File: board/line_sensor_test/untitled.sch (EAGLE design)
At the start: 92 parts, among them U1 74HC4067SSOP-24, U2 74HC4067SSOP-24

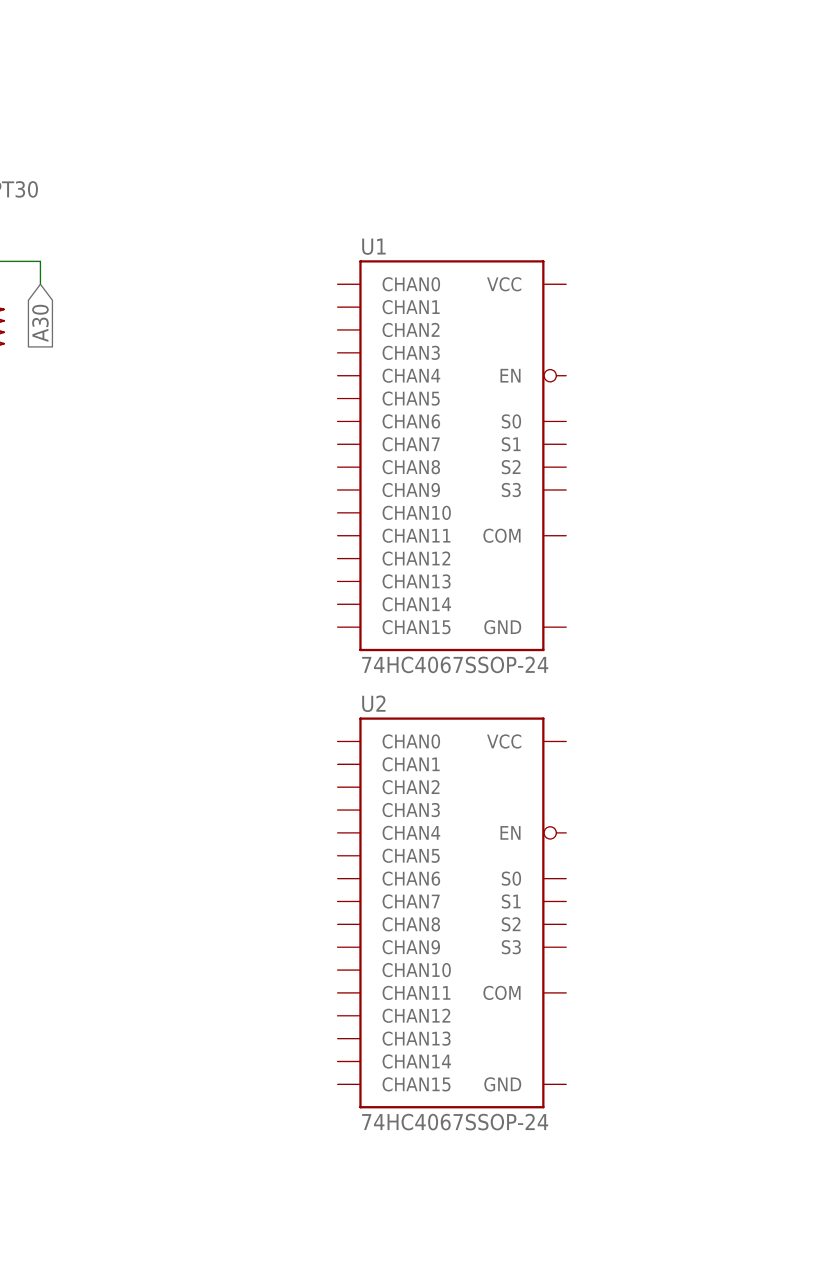
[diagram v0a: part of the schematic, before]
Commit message: making linesonsor_2
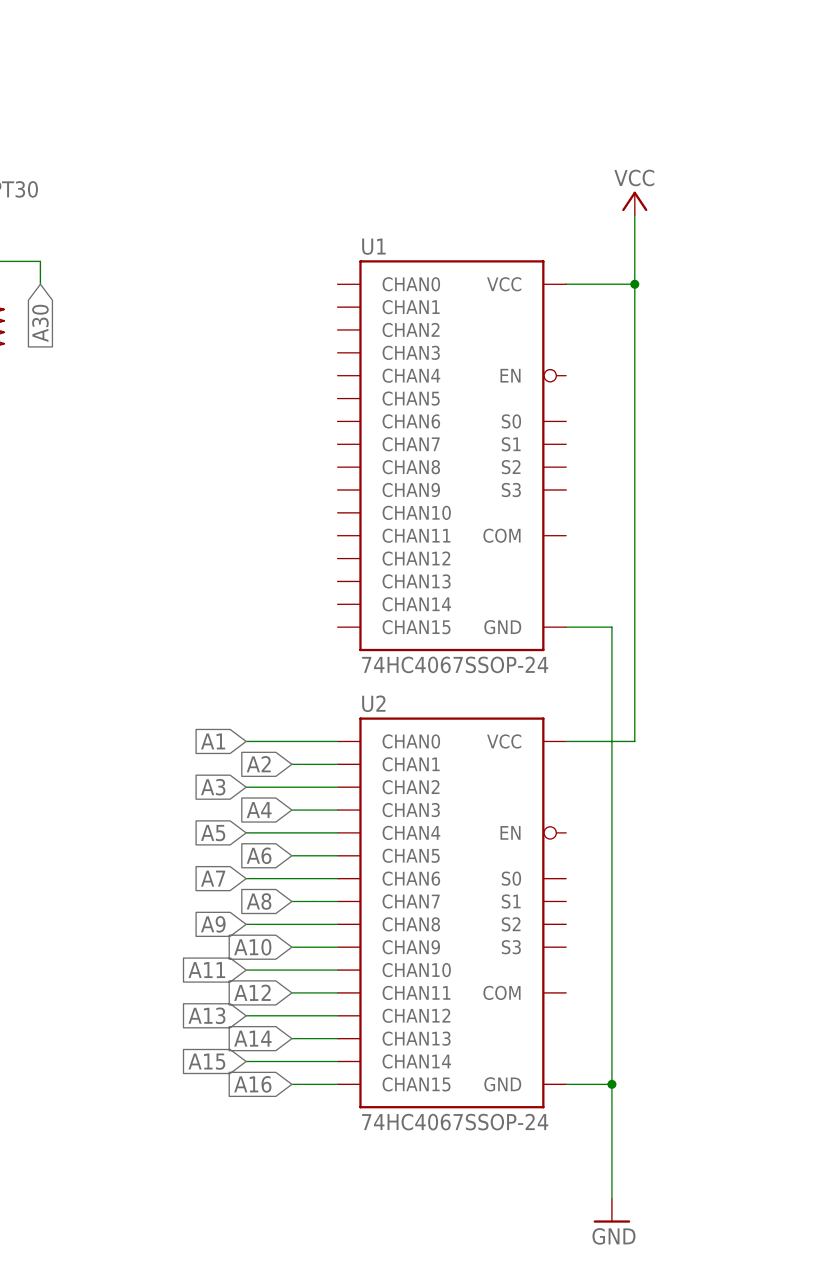
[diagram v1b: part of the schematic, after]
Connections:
- net A1: now also U2.CHAN0
- net A10: now also U2.CHAN9
- net A11: now also U2.CHAN10
- net A12: now also U2.CHAN11
- net A13: now also U2.CHAN12
- net A14: now also U2.CHAN13
- net A15: now also U2.CHAN14
- net A16: now also U2.CHAN15
- net A2: now also U2.CHAN1
- net A3: now also U2.CHAN2
- net A4: now also U2.CHAN3
- net A5: now also U2.CHAN4
- net A6: now also U2.CHAN5
- net A7: now also U2.CHAN6
- net A8: now also U2.CHAN7
- net A9: now also U2.CHAN8
- net GND: now also U1.GND, U2.GND
- net VCC: now also U1.VCC, U2.VCC
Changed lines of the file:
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@@
 <part name="U1" library="74HC4067" deviceset="74HC4067" device="SSOP-24"/>
 <part name="U2" library="74HC4067" deviceset="74HC4067" device="SSOP-24"/>
+<part name="U$3" library="supply" deviceset="VCC" device=""/>
+<part name="GND3" library="supply" deviceset="GND" device=""/>
 </parts>
 <sheets>
@@
 <attribute name="VALUE" x="365.76" y="-99.06" size="1.778" layer="95"/>
 </instance>
+<instance part="U$3" gate="G$1" x="396.24" y="5.08" smashed="yes">
+<attribute name="VALUE" x="393.954" y="5.842" size="1.778" layer="96" font="vector"/>
+</instance>
+<instance part="GND3" gate="1" x="393.7" y="-109.22" smashed="yes">
+<attribute name="VALUE" x="391.414" y="-111.76" size="1.778" layer="96" font="vector"/>
+</instance>
 </instances>
 <busses>
@@
 <label x="35.56" y="-5.08" size="1.778" layer="95" rot="R270" xref="yes"/>
 </segment>
+<segment>
+<pinref part="U2" gate="G$1" pin="CHAN0"/>
+<wire x1="363.22" y1="-55.88" x2="353.06" y2="-55.88" width="0.1524" layer="91"/>
+<label x="353.06" y="-55.88" size="1.778" layer="95" rot="R180" xref="yes"/>
+</segment>
 </net>
 <net name="A2" class="0">
@@
 <junction x="40.64" y="-2.54"/>
 </segment>
+<segment>
+<pinref part="U2" gate="G$1" pin="CHAN1"/>
+<wire x1="363.22" y1="-58.42" x2="358.14" y2="-58.42" width="0.1524" layer="91"/>
+<label x="358.14" y="-58.42" size="1.778" layer="95" rot="R180" xref="yes"/>
+</segment>
 </net>
 <net name="A3" class="0">
@@
 <junction x="50.8" y="-2.54"/>
 </segment>
+<segment>
+<pinref part="U2" gate="G$1" pin="CHAN2"/>
+<wire x1="363.22" y1="-60.96" x2="353.06" y2="-60.96" width="0.1524" layer="91"/>
+<label x="353.06" y="-60.96" size="1.778" layer="95" rot="R180" xref="yes"/>
+</segment>
 </net>
 <net name="A4" class="0">
@@
 <wire x1="66.04" y1="-2.54" x2="66.04" y2="-5.08" width="0.1524" layer="91"/>
 </segment>
+<segment>
+<pinref part="U2" gate="G$1" pin="CHAN3"/>
+<wire x1="363.22" y1="-63.5" x2="358.14" y2="-63.5" width="0.1524" layer="91"/>
+<label x="358.14" y="-63.5" size="1.778" layer="95" rot="R180" xref="yes"/>
+</segment>
 </net>
 <net name="A5" class="0">
@@
 <junction x="71.12" y="-2.54"/>
 <wire x1="76.2" y1="-2.54" x2="76.2" y2="-5.08" width="0.1524" layer="91"/>
+</segment>
+<segment>
+<pinref part="U2" gate="G$1" pin="CHAN4"/>
+<wire x1="363.22" y1="-66.04" x2="353.06" y2="-66.04" width="0.1524" layer="91"/>
+<label x="353.06" y="-66.04" size="1.778" layer="95" rot="R180" xref="yes"/>
 </segment>
 </net>
@@
 <junction x="635" y="81.28"/>
 </segment>
+<segment>
+<pinref part="U2" gate="G$1" pin="VCC"/>
+<wire x1="388.62" y1="-55.88" x2="396.24" y2="-55.88" width="0.1524" layer="91"/>
+<wire x1="396.24" y1="-55.88" x2="396.24" y2="-5.08" width="0.1524" layer="91"/>
+<pinref part="U1" gate="G$1" pin="VCC"/>
+<wire x1="396.24" y1="2.54" x2="396.24" y2="-5.08" width="0.1524" layer="91"/>
+<wire x1="396.24" y1="-5.08" x2="388.62" y2="-5.08" width="0.1524" layer="91"/>
+<junction x="396.24" y="-5.08"/>
+<pinref part="U$3" gate="G$1" pin="VCC"/>
+</segment>
 </net>
 <net name="A6" class="0">
@@
 <junction x="81.28" y="-2.54"/>
 </segment>
+<segment>
+<pinref part="U2" gate="G$1" pin="CHAN5"/>
+<wire x1="363.22" y1="-68.58" x2="358.14" y2="-68.58" width="0.1524" layer="91"/>
+<label x="358.14" y="-68.58" size="1.778" layer="95" rot="R180" xref="yes"/>
+</segment>
 </net>
 <net name="A7" class="0">
@@
 <wire x1="96.52" y1="-2.54" x2="96.52" y2="-5.08" width="0.1524" layer="91"/>
 </segment>
+<segment>
+<pinref part="U2" gate="G$1" pin="CHAN6"/>
+<wire x1="363.22" y1="-71.12" x2="353.06" y2="-71.12" width="0.1524" layer="91"/>
+<label x="353.06" y="-71.12" size="1.778" layer="95" rot="R180" xref="yes"/>
+</segment>
 </net>
 <net name="A8" class="0">
@@
 <junction x="101.6" y="-2.54"/>
 </segment>
+<segment>
+<label x="358.14" y="-73.66" size="1.778" layer="95" rot="R180" xref="yes"/>
+<wire x1="360.5276" y1="-73.66" x2="358.14" y2="-73.66" width="0.1524" layer="91"/>
+<pinref part="U2" gate="G$1" pin="CHAN7"/>
+<wire x1="360.5276" y1="-73.66" x2="363.22" y2="-73.66" width="0.1524" layer="91"/>
+</segment>
 </net>
 <net name="A9" class="0">
@@
 <junction x="111.76" y="-2.54"/>
 </segment>
+<segment>
+<pinref part="U2" gate="G$1" pin="CHAN8"/>
+<wire x1="363.22" y1="-76.2" x2="353.06" y2="-76.2" width="0.1524" layer="91"/>
+<label x="353.06" y="-76.2" size="1.778" layer="95" rot="R180" xref="yes"/>
+</segment>
 </net>
 <net name="A10" class="0">
@@
 <junction x="121.92" y="-2.54"/>
 </segment>
+<segment>
+<pinref part="U2" gate="G$1" pin="CHAN9"/>
+<wire x1="363.22" y1="-78.74" x2="358.14" y2="-78.74" width="0.1524" layer="91"/>
+<label x="358.14" y="-78.74" size="1.778" layer="95" rot="R180" xref="yes"/>
+</segment>
 </net>
 <net name="A11" class="0">
@@
 <junction x="132.08" y="-2.54"/>
 </segment>
+<segment>
+<pinref part="U2" gate="G$1" pin="CHAN10"/>
+<wire x1="363.22" y1="-81.28" x2="353.06" y2="-81.28" width="0.1524" layer="91"/>
+<label x="353.06" y="-81.28" size="1.778" layer="95" rot="R180" xref="yes"/>
+</segment>
 </net>
 <net name="A12" class="0">
@@
 <junction x="142.24" y="-2.54"/>
 </segment>
+<segment>
+<pinref part="U2" gate="G$1" pin="CHAN11"/>
+<wire x1="363.22" y1="-83.82" x2="358.14" y2="-83.82" width="0.1524" layer="91"/>
+<label x="358.14" y="-83.82" size="1.778" layer="95" rot="R180" xref="yes"/>
+</segment>
 </net>
 <net name="A13" class="0">
@@
 <junction x="152.4" y="-2.54"/>
 </segment>
+<segment>
+<pinref part="U2" gate="G$1" pin="CHAN12"/>
+<wire x1="363.22" y1="-86.36" x2="353.06" y2="-86.36" width="0.1524" layer="91"/>
+<label x="353.06" y="-86.36" size="1.778" layer="95" rot="R180" xref="yes"/>
+</segment>
 </net>
 <net name="A14" class="0">
@@
 <junction x="162.56" y="-2.54"/>
 </segment>
+<segment>
+<pinref part="U2" gate="G$1" pin="CHAN13"/>
+<wire x1="363.22" y1="-88.9" x2="358.14" y2="-88.9" width="0.1524" layer="91"/>
+<label x="358.14" y="-88.9" size="1.778" layer="95" rot="R180" xref="yes"/>
+</segment>
 </net>
 <net name="A15" class="0">
@@
 <junction x="172.72" y="-2.54"/>
 </segment>
+<segment>
+<pinref part="U2" gate="G$1" pin="CHAN14"/>
+<wire x1="363.22" y1="-91.44" x2="353.06" y2="-91.44" width="0.1524" layer="91"/>
+<label x="353.06" y="-91.44" size="1.778" layer="95" rot="R180" xref="yes"/>
+</segment>
 </net>
 <net name="A16" class="0">
@@
 <wire x1="187.96" y1="-2.54" x2="182.88" y2="-2.54" width="0.1524" layer="91"/>
 <junction x="182.88" y="-2.54"/>
+</segment>
+<segment>
+<pinref part="U2" gate="G$1" pin="CHAN15"/>
+<wire x1="363.22" y1="-93.98" x2="358.14" y2="-93.98" width="0.1524" layer="91"/>
+<label x="358.14" y="-93.98" size="1.778" layer="95" rot="R180" xref="yes"/>
 </segment>
 </net>
@@
 <junction x="629.92" y="50.8"/>
 </segment>
-</net>
+<segment>
+<pinref part="U1" gate="G$1" pin="GND"/>
+<wire x1="388.62" y1="-43.18" x2="393.7" y2="-43.18" width="0.1524" layer="91"/>
+<pinref part="U2" gate="G$1" pin="GND"/>
+<wire x1="393.7" y1="-43.18" x2="393.7" y2="-93.98" width="0.1524" layer="91"/>
+<wire x1="393.7" y1="-93.98" x2="388.62" y2="-93.98" width="0.1524" layer="91"/>
+<wire x1="393.7" y1="-93.98" x2="393.7" y2="-106.68" width="0.1524" layer="91"/>
+<junction x="393.7" y="-93.98"/>
+<pinref part="GND3" gate="1" pin="GND"/>
+</segment>
+</net>

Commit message: making linesensor_3
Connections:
- removed net GND1: R1.1, R10.1, R11.1, R12.1, R13.1, R14.1, R15.1, R16.1, R17.1, R18.1, R19.1, R2.1, R20.1, R21.1, R22.1, R23.1, R24.1, R25.1, R26.1, R27.1, R28.1, R29.1, R3.1, R30.1, R4.1, R5.1, R6.1, R7.1, R8.1, R9.1
- net GND: now also R1.1, R10.1, R11.1, R12.1, R13.1, R14.1, R15.1, R16.1, R17.1, R18.1, R19.1, R2.1, R20.1, R21.1, R22.1, R23.1, R24.1, R25.1, R26.1, R27.1, R28.1, R29.1, R3.1, R30.1, R4.1, R5.1, R6.1, R7.1, R8.1, R9.1

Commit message: put resister
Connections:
- net A24: now also U1.CHAN8
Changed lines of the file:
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@@
 <?xml version="1.0" encoding="utf-8"?>
 <!DOCTYPE eagle SYSTEM "eagle.dtd">
-<eagle version="9.6.1">
+<eagle version="9.6.2">
 <drawing>
 <settings>
@@
 <junction x="264.16" y="-2.54"/>
 </segment>
-</net>
+<segment>
+<pinref part="U1" gate="G$1" pin="CHAN8"/>
+<wire x1="363.22" y1="-25.4" x2="358.14" y2="-25.4" width="0.1524" layer="91"/>
+<label x="358.14" y="-25.4" size="1.778" layer="95" rot="R180" xref="yes"/>
+</segment>
+</net>

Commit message: Making linesensor
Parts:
- added SV1: (no value), con-lstb:MA06-2
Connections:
- new net AIN0: U1.COM
- new net AIN1: SV1.11, U2.COM
- new net N$10: SV1.7, U2.S3
- new net N$11: SV1.9, U2.S2
- new net N$13: SV1.10, U2.S1
- new net N$14: SV1.12, U2.S0
- new net N$15: U1.CHAN5
- new net N$5: U1.S0
- new net N$7: U1.S1
- new net N$8: U1.S2
- new net N$9: U1.S3
- net A22: now also U1.CHAN6
- net A23: now also U1.CHAN7
- net GND: now also SV1.8, U1.EN, U2.EN
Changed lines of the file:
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@@
 <part name="GND3" library="supply" deviceset="GND" device=""/>
 <part name="GND1" library="supply" deviceset="GND" device=""/>
+<part name="SV1" library="con-lstb" library_urn="urn:adsk.eagle:library:162" deviceset="MA06-2" device="" package3d_urn="urn:adsk.eagle:package:8342/1"/>
+<part name="GND4" library="supply" deviceset="GND" device=""/>
 </parts>
 <sheets>
@@
 <instance part="GND1" gate="1" x="25.4" y="-22.86" smashed="yes">
 <attribute name="VALUE" x="23.114" y="-25.4" size="1.778" layer="96" font="vector"/>
+</instance>
+<instance part="SV1" gate="1" x="447.04" y="-48.26" smashed="yes" rot="R180">
+<attribute name="VALUE" x="450.85" y="-35.56" size="1.778" layer="96" rot="R180"/>
+<attribute name="NAME" x="450.85" y="-56.642" size="1.778" layer="95" rot="R180"/>
+</instance>
+<instance part="GND4" gate="1" x="464.82" y="-58.42" smashed="yes">
+<attribute name="VALUE" x="462.534" y="-60.96" size="1.778" layer="96" font="vector"/>
 </instance>
 </instances>
@@
 <junction x="243.84" y="-2.54"/>
 </segment>
+<segment>
+<pinref part="U1" gate="G$1" pin="CHAN6"/>
+<wire x1="363.22" y1="-20.32" x2="358.14" y2="-20.32" width="0.1524" layer="91"/>
+<label x="358.14" y="-20.32" size="1.778" layer="95" rot="R180" xref="yes"/>
+</segment>
 </net>
 <net name="A23" class="0">
@@
 <wire x1="259.08" y1="-2.54" x2="254" y2="-2.54" width="0.1524" layer="91"/>
 <junction x="254" y="-2.54"/>
+</segment>
+<segment>
+<pinref part="U1" gate="G$1" pin="CHAN7"/>
+<wire x1="363.22" y1="-22.86" x2="350.52" y2="-22.86" width="0.1524" layer="91"/>
+<label x="350.52" y="-22.86" size="1.778" layer="95" rot="R180" xref="yes"/>
 </segment>
 </net>
@@
 <wire x1="388.62" y1="-43.18" x2="393.7" y2="-43.18" width="0.1524" layer="91"/>
 <pinref part="U2" gate="G$1" pin="GND"/>
-<wire x1="393.7" y1="-43.18" x2="393.7" y2="-93.98" width="0.1524" layer="91"/>
+<wire x1="393.7" y1="-43.18" x2="393.7" y2="-66.04" width="0.1524" layer="91"/>
+<wire x1="393.7" y1="-66.04" x2="393.7" y2="-93.98" width="0.1524" layer="91"/>
 <wire x1="393.7" y1="-93.98" x2="388.62" y2="-93.98" width="0.1524" layer="91"/>
 <wire x1="393.7" y1="-93.98" x2="393.7" y2="-106.68" width="0.1524" layer="91"/>
 <junction x="393.7" y="-93.98"/>
 <pinref part="GND3" gate="1" pin="GND"/>
+<pinref part="U2" gate="G$1" pin="EN"/>
+<wire x1="388.62" y1="-66.04" x2="393.7" y2="-66.04" width="0.1524" layer="91"/>
+<junction x="393.7" y="-66.04"/>
+<pinref part="U1" gate="G$1" pin="EN"/>
+<wire x1="393.7" y1="-43.18" x2="393.7" y2="-15.24" width="0.1524" layer="91"/>
+<wire x1="393.7" y1="-15.24" x2="388.62" y2="-15.24" width="0.1524" layer="91"/>
+<junction x="393.7" y="-43.18"/>
 </segment>
 <segment>
@@
 <pinref part="GND1" gate="1" pin="GND"/>
 </segment>
+<segment>
+<pinref part="SV1" gate="1" pin="8"/>
+<wire x1="454.66" y1="-48.26" x2="464.82" y2="-48.26" width="0.1524" layer="91"/>
+<wire x1="464.82" y1="-48.26" x2="464.82" y2="-55.88" width="0.1524" layer="91"/>
+<pinref part="GND4" gate="1" pin="GND"/>
+</segment>
 </net>
 <net name="N$6" class="0">
@@
 <pinref part="LED1" gate="G$1" pin="DI"/>
 <wire x1="7.62" y1="63.5" x2="-2.54" y2="63.5" width="0.1524" layer="91"/>
+</segment>
+</net>
+<net name="N$5" class="0">
+<segment>
+<pinref part="U1" gate="G$1" pin="S0"/>
+<wire x1="388.62" y1="-20.32" x2="441.96" y2="-20.32" width="0.1524" layer="91"/>
+</segment>
+</net>
+<net name="N$7" class="0">
+<segment>
+<pinref part="U1" gate="G$1" pin="S1"/>
+<wire x1="388.62" y1="-22.86" x2="439.42" y2="-22.86" width="0.1524" layer="91"/>
+</segment>
+</net>
+<net name="N$8" class="0">
+<segment>
+<pinref part="U1" gate="G$1" pin="S2"/>
+<wire x1="388.62" y1="-25.4" x2="436.88" y2="-25.4" width="0.1524" layer="91"/>
+</segment>
+</net>
+<net name="N$9" class="0">
+<segment>
+<pinref part="U1" gate="G$1" pin="S3"/>
+<wire x1="388.62" y1="-27.94" x2="434.34" y2="-27.94" width="0.1524" layer="91"/>
+</segment>
+</net>
+<net name="AIN1" class="0">
+<segment>
+<pinref part="U2" gate="G$1" pin="COM"/>
+<wire x1="388.62" y1="-83.82" x2="431.8" y2="-83.82" width="0.1524" layer="91"/>
+<pinref part="SV1" gate="1" pin="11"/>
+<wire x1="431.8" y1="-83.82" x2="431.8" y2="-53.34" width="0.1524" layer="91"/>
+<wire x1="431.8" y1="-53.34" x2="439.42" y2="-53.34" width="0.1524" layer="91"/>
+</segment>
+</net>
+<net name="AIN0" class="0">
+<segment>
+<pinref part="U1" gate="G$1" pin="COM"/>
+<wire x1="388.62" y1="-33.02" x2="431.8" y2="-33.02" width="0.1524" layer="91"/>
+</segment>
+</net>
+<net name="N$10" class="0">
+<segment>
+<pinref part="U2" gate="G$1" pin="S3"/>
+<wire x1="388.62" y1="-78.74" x2="434.34" y2="-78.74" width="0.1524" layer="91"/>
+<pinref part="SV1" gate="1" pin="7"/>
+<wire x1="439.42" y1="-48.26" x2="434.34" y2="-48.26" width="0.1524" layer="91"/>
+<wire x1="434.34" y1="-48.26" x2="434.34" y2="-78.74" width="0.1524" layer="91"/>
+</segment>
+</net>
+<net name="N$11" class="0">
+<segment>
+<pinref part="U2" gate="G$1" pin="S2"/>
+<wire x1="388.62" y1="-76.2" x2="436.88" y2="-76.2" width="0.1524" layer="91"/>
+<pinref part="SV1" gate="1" pin="9"/>
+<wire x1="439.42" y1="-50.8" x2="436.88" y2="-50.8" width="0.1524" layer="91"/>
+<wire x1="436.88" y1="-50.8" x2="436.88" y2="-76.2" width="0.1524" layer="91"/>
+</segment>
+</net>
+<net name="N$13" class="0">
+<segment>
+<pinref part="U2" gate="G$1" pin="S1"/>
+<wire x1="388.62" y1="-73.66" x2="459.74" y2="-73.66" width="0.1524" layer="91"/>
+<pinref part="SV1" gate="1" pin="10"/>
+<wire x1="454.66" y1="-50.8" x2="459.74" y2="-50.8" width="0.1524" layer="91"/>
+<wire x1="459.74" y1="-50.8" x2="459.74" y2="-73.66" width="0.1524" layer="91"/>
+</segment>
+</net>
+<net name="N$14" class="0">
+<segment>
+<pinref part="U2" gate="G$1" pin="S0"/>
+<wire x1="388.62" y1="-71.12" x2="457.2" y2="-71.12" width="0.1524" layer="91"/>
+<wire x1="457.2" y1="-71.12" x2="457.2" y2="-53.34" width="0.1524" layer="91"/>
+<pinref part="SV1" gate="1" pin="12"/>
+<wire x1="457.2" y1="-53.34" x2="454.66" y2="-53.34" width="0.1524" layer="91"/>
+</segment>
+</net>
+<net name="N$15" class="0">
+<segment>
+<pinref part="U1" gate="G$1" pin="CHAN5"/>
+<wire x1="363.22" y1="-17.78" x2="350.52" y2="-17.78" width="0.1524" layer="91"/>
 </segment>
 </net>
@@
 </schematic>
 </drawing>
+<compatibility>
+<note version="8.2" severity="warning">
+Since Version 8.2, EAGLE supports online libraries. The ids
+of those online libraries will not be understood (or retained)
+with this version.
+</note>
+<note version="8.3" severity="warning">
+Since Version 8.3, EAGLE supports URNs for individual library
+assets (packages, symbols, and devices). The URNs of those assets
+will not be understood (or retained) with this version.
+</note>
+<note version="8.3" severity="warning">
+Since Version 8.3, EAGLE supports the association of 3D packages
+with devices in libraries, schematics, and board files. Those 3D
+packages will not be understood (or retained) with this version.
+</note>
+</compatibility>
 </eagle>

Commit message: update linesensor
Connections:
- removed net N$15: U1.CHAN5
- net A16: now also U1.CHAN0
- net A17: now also U1.CHAN1
- net A18: now also U1.CHAN2
- net A19: now also U1.CHAN3
- net A20: now also U1.CHAN4
- net A21: now also U1.CHAN5
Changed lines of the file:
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@@
 <label x="358.14" y="-93.98" size="1.778" layer="95" rot="R180" xref="yes"/>
+</segment>
+<segment>
+<pinref part="U1" gate="G$1" pin="CHAN0"/>
+<wire x1="363.22" y1="-5.08" x2="358.14" y2="-5.08" width="0.1524" layer="91"/>
+<label x="358.14" y="-5.08" size="1.778" layer="95" rot="R180" xref="yes"/>
 </segment>
 </net>
@@
 <junction x="193.04" y="-2.54"/>
 </segment>
+<segment>
+<pinref part="U1" gate="G$1" pin="CHAN1"/>
+<wire x1="363.22" y1="-7.62" x2="350.52" y2="-7.62" width="0.1524" layer="91"/>
+<label x="350.52" y="-7.62" size="1.778" layer="95" rot="R180" xref="yes"/>
+</segment>
 </net>
 <net name="A18" class="0">
@@
 <junction x="203.2" y="-2.54"/>
 </segment>
+<segment>
+<pinref part="U1" gate="G$1" pin="CHAN2"/>
+<wire x1="363.22" y1="-10.16" x2="358.14" y2="-10.16" width="0.1524" layer="91"/>
+<label x="358.14" y="-10.16" size="1.778" layer="95" rot="R180" xref="yes"/>
+</segment>
 </net>
 <net name="A19" class="0">
@@
 <junction x="213.36" y="-2.54"/>
 </segment>
+<segment>
+<pinref part="U1" gate="G$1" pin="CHAN3"/>
+<wire x1="363.22" y1="-12.7" x2="350.52" y2="-12.7" width="0.1524" layer="91"/>
+<label x="350.52" y="-12.7" size="1.778" layer="95" rot="R180" xref="yes"/>
+</segment>
 </net>
 <net name="A20" class="0">
@@
 <junction x="223.52" y="-2.54"/>
 </segment>
+<segment>
+<pinref part="U1" gate="G$1" pin="CHAN4"/>
+<wire x1="363.22" y1="-15.24" x2="358.14" y2="-15.24" width="0.1524" layer="91"/>
+<label x="358.14" y="-15.24" size="1.778" layer="95" rot="R180" xref="yes"/>
+</segment>
 </net>
 <net name="A21" class="0">
@@
 <wire x1="238.76" y1="-2.54" x2="233.68" y2="-2.54" width="0.1524" layer="91"/>
 <junction x="233.68" y="-2.54"/>
+</segment>
+<segment>
+<pinref part="U1" gate="G$1" pin="CHAN5"/>
+<wire x1="363.22" y1="-17.78" x2="350.52" y2="-17.78" width="0.1524" layer="91"/>
+<label x="350.52" y="-17.78" size="1.778" layer="95" rot="R180" xref="yes"/>
 </segment>
 </net>
@@
 </segment>
 </net>
-<net name="N$15" class="0">
-<segment>
-<pinref part="U1" gate="G$1" pin="CHAN5"/>
-<wire x1="363.22" y1="-17.78" x2="350.52" y2="-17.78" width="0.1524" layer="91"/>
-</segment>
-</net>
